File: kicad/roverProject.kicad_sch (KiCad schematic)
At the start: 8 parts, among them M1 DC Motor w/ Encoder, M2 DC Motor w/ Encoder, U1 MPU-6050

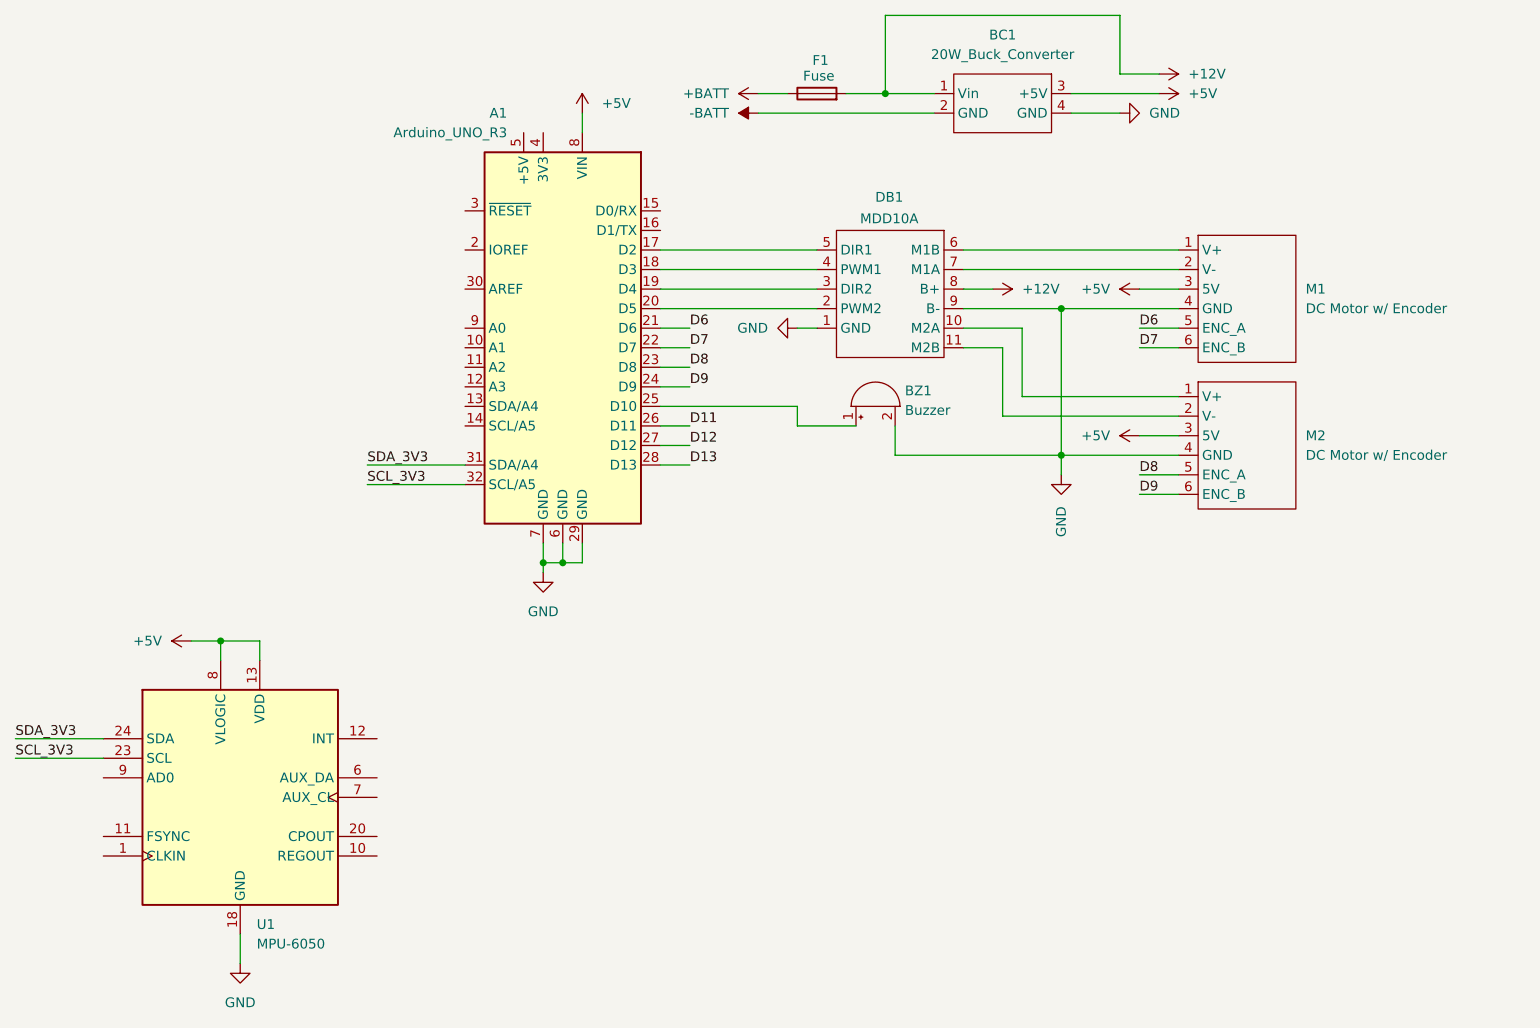
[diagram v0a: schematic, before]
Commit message: Repo Refactoring
General tidying of the docs and putting files where they need to be.

No code edited, only moved.
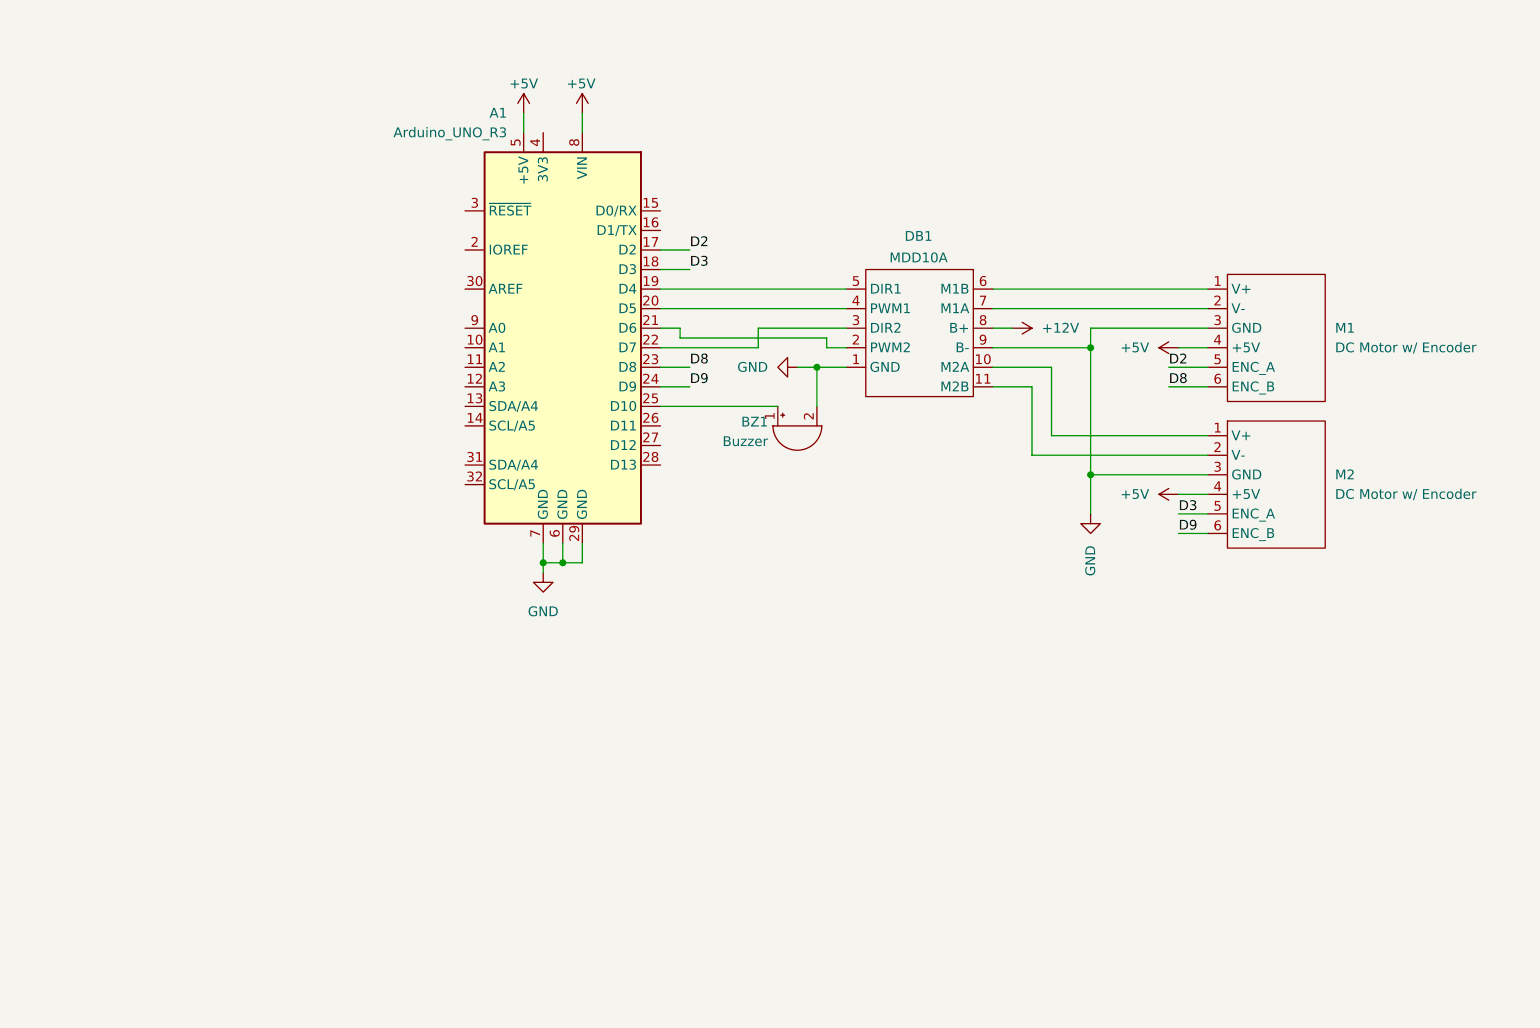
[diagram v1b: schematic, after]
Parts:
- removed BC1: 20W_Buck_Converter, symbol roverProjectLib:20W_Buck_Converter
- removed F1: Fuse, symbol Device:Fuse
- removed U1: MPU-6050, Sensor_Motion:InvenSense_QFN-24_4x4mm_P0.5mm, symbol Sensor_Motion:MPU-6050
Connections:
- net +5V: now also A1.5 (+5V), M1.4 (+5V), M2.4 (+5V); no longer M1.3 (5V), M2.3 (5V)
- net D8: now also M1.6 (ENC_B); no longer M2.5 (ENC_A)
- net GND: now also M1.3 (GND), M2.3 (GND); no longer M1.4 (GND), M2.4 (GND)
- net at DB1.5 (DIR1): now also A1.19 (D4); no longer A1.17 (D2)
- net at DB1.4 (PWM1): now also A1.20 (D5); no longer A1.18 (D3)
- net at DB1.3 (DIR2): now also A1.22 (D7); no longer A1.19 (D4)
- net at DB1.2 (PWM2): now also A1.21 (D6); no longer A1.20 (D5)
- net D11: no longer names the net of A1.26 (D11)
- net D12: no longer names the net of A1.27 (D12)
- net D13: no longer names the net of A1.28 (D13)
- net D6 renamed D2
- net D2: now also A1.17 (D2); no longer A1.21 (D6)
- removed net D7: A1.22 (D7), M1.6 (ENC_B)
- net SCL_3V3: no longer names the net of A1.32 (SCL/A5)
- net SDA_3V3: no longer names the net of A1.31 (SDA/A4)
- new net D3: A1.18 (D3), M2.5 (ENC_A)
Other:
- moved on the sheet: DB1, M1, M2
